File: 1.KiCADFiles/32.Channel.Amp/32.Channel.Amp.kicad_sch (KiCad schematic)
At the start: 4 parts

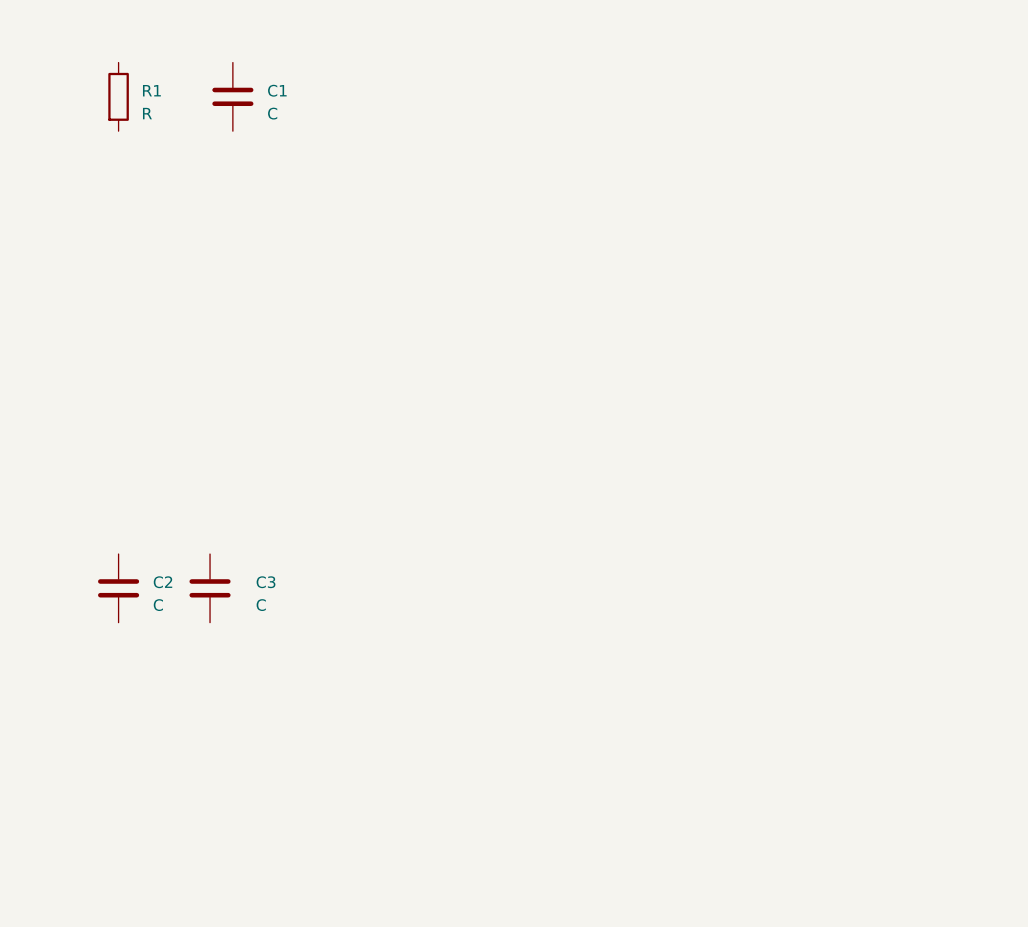
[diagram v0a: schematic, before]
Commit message: Created 16 Channel Box
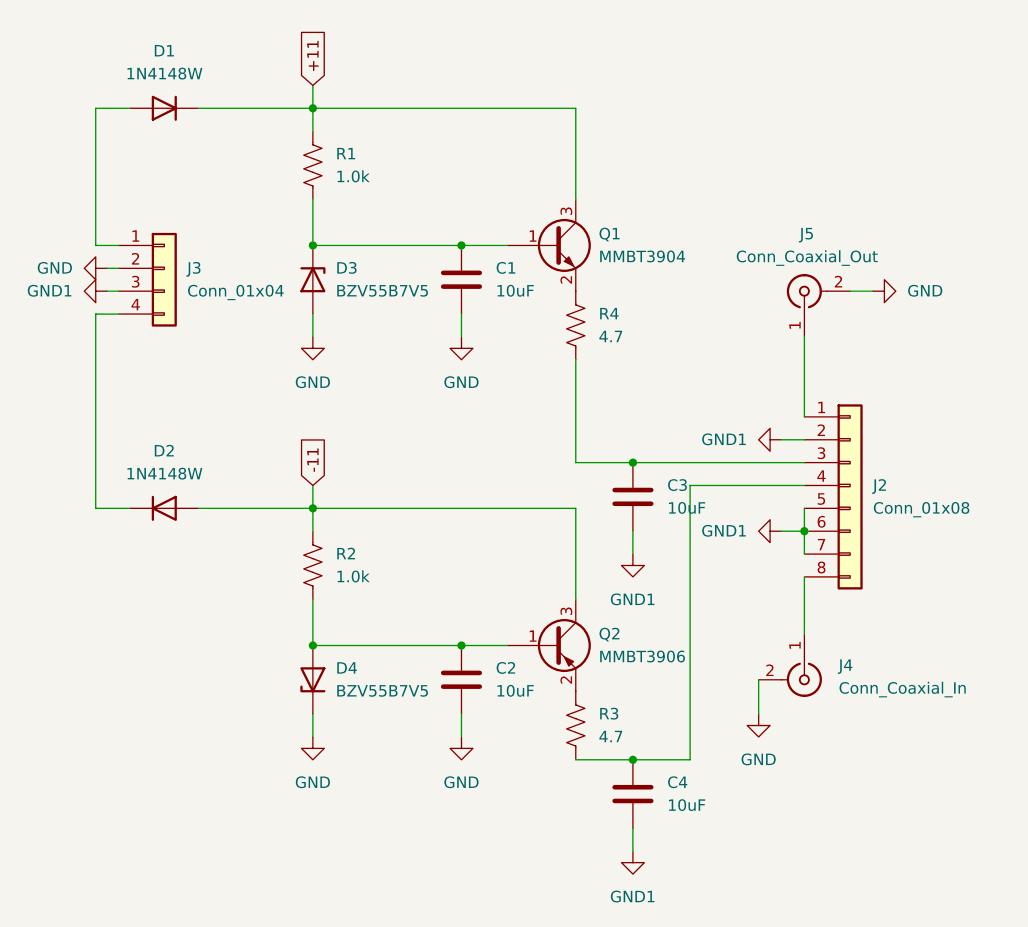
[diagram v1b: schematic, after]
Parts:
- removed R1: R, symbol Device:R
- added C4: 10uF, Capacitor_SMD:C_1206_3216Metric_Pad1.33x1.80mm_HandSolder, symbol Device:C
- added D1, D2: 1N4148W, Diode_SMD:D_SOD-123, symbol Diode:1N4148W
- added D3, D4: BZV55B7V5, Diode_SMD:D_MiniMELF, symbol Diode:BZV55B7V5
- added J2: Conn_01x08, Connector_PinSocket_2.54mm:PinSocket_1x08_P2.54mm_Vertical, symbol Connector_Generic:Conn_01x08
- added J3: Conn_01x04, Connector_PinSocket_2.54mm:PinSocket_1x04_P2.54mm_Vertical, symbol Connector_Generic:Conn_01x04
- added J4: Conn_Coaxial_In, Connector_Coaxial:SMA_Amphenol_901-144_Vertical, symbol Connector:Conn_Coaxial
- added J5: Conn_Coaxial_Out, Connector_Coaxial:SMA_Amphenol_901-144_Vertical, symbol Connector:Conn_Coaxial
- added Q1: MMBT3904, Package_TO_SOT_SMD:SOT-23, symbol Transistor_BJT:MMBT3904
- added Q2: MMBT3906, Package_TO_SOT_SMD:SOT-23, symbol Transistor_BJT:MMBT3906
- added R1, R2: 1.0k, Resistor_SMD:R_1206_3216Metric_Pad1.30x1.75mm_HandSolder, symbol Device:R_US
- added R3, R4: 4.7, Resistor_SMD:R_1206_3216Metric_Pad1.30x1.75mm_HandSolder, symbol Device:R_US
- C1, C2, C3: value C -> 10uF; footprint (none) -> Capacitor_SMD:C_1206_3216Metric_Pad1.33x1.80mm_HandSolder
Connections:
- net at C3.1: now also J2.3 (Pin_3), R4.2
- net GND1: now reaches C3.2
- net GND1: now also C4.2, J2.2 (GND), J2.5 (Pin_5), J2.6 (Pin_6), J2.7 (Pin_7), J3.3 (Pin_3)
- net at C1.1: now also D3.1 (K), Q1.1 (B), R1.2
- net GND: now reaches C1.2
- net GND: now also C2.2, D3.2 (A), D4.1 (K), J3.2 (Pin_2), J4.2 (Ext), J5.2 (Ext)
- net at C2.1: now also D4.2 (A), Q2.1 (B), R2.2
- new net: C4.1, J2.4 (Pin_4), R3.2
- new net: Q2.2 (E), R3.1
- new net: D1.2 (A), J3.1 (Pin_1)
- new net: J2.8 (Input), J4.1 (In)
- new net: J2.1 (Output), J5.1 (In)
- new net: D2.1 (K), J3.4 (Pin_4)
- new net: Q1.2 (E), R4.1
- new net +11: D1.1 (K), Q1.3 (C), R1.1
- new net -11: D2.2 (A), Q2.3 (C), R2.1

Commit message: Updated 32 Channel Format, Included Chip Board
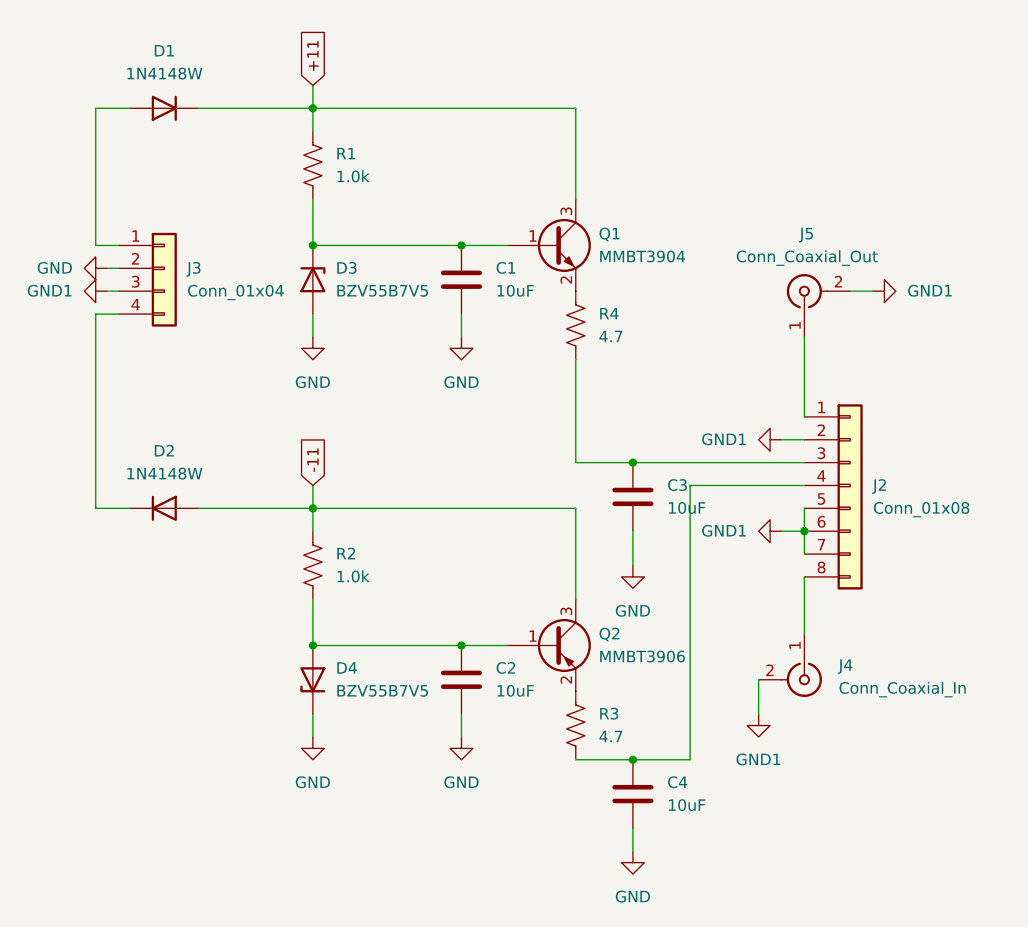
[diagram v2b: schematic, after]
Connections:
- net GND: now also C3.2, C4.2; no longer J4.2 (Ext), J5.2 (Ext)
- net GND1: now also J4.2 (Ext), J5.2 (Ext); no longer C3.2, C4.2
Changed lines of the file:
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@@
     (stroke (width 0) (type default))
   )
-  (wire (pts (xy 99.06 86.36) (xy 99.06 83.82))
+  (wire (pts (xy 99.06 87.63) (xy 99.06 83.82))
     (stroke (width 0) (type default))
   )
@@
     )
   )
+  (symbol (lib_id "power:GND1") (at 125.73 57.15 90) (unit 1)
+    (in_bom yes) (on_board yes) (dnp no) (fields_autoplaced)
+    (property "Reference" "#PWR011" (at 132.08 57.15 0)
+      (effects (font (size 1.27 1.27)) hide)
+    )
+    (property "Value" "GND1" (at 129.54 57.15 90)
+      (effects (font (size 1.27 1.27)) (justify right))
+    )
+    (property "Footprint" "" (at 125.73 57.15 0)
+      (effects (font (size 1.27 1.27)) hide)
+    )
+    (property "Datasheet" "" (at 125.73 57.15 0)
+      (effects (font (size 1.27 1.27)) hide)
+    )
+    (pin "1")
+    (instances
+      (project "Single.Channel.Amp"
+        (path "/08e8a37f-dc9c-4c12-ad59-7a5b52f61be7"
+          (reference "#PWR011") (unit 1)
+        )
+      )
+      (project "32.Channel.Amp"
+        (path "/13fa3f73-84bf-4039-afd1-d465267c6ba6"
+          (reference "#PWR08") (unit 1)
+        )
+      )
+    )
+  )
   (symbol (lib_id "Device:C") (at 99.06 113.03 0) (unit 1)
     (in_bom yes) (on_board yes) (dnp no) (fields_autoplaced)
@@
     )
   )
+  (symbol (lib_id "power:GND") (at 99.06 87.63 0) (unit 1)
+    (in_bom yes) (on_board yes) (dnp no) (fields_autoplaced)
+    (property "Reference" "#PWR02" (at 99.06 93.98 0)
+      (effects (font (size 1.27 1.27)) hide)
+    )
+    (property "Value" "GND" (at 99.06 92.71 0)
+      (effects (font (size 1.27 1.27)))
+    )
+    (property "Footprint" "" (at 99.06 87.63 0)
+      (effects (font (size 1.27 1.27)) hide)
+    )
+    (property "Datasheet" "" (at 99.06 87.63 0)
+      (effects (font (size 1.27 1.27)) hide)
+    )
+    (pin "1")
+    (instances
+      (project "Single.Channel.Amp"
+        (path "/08e8a37f-dc9c-4c12-ad59-7a5b52f61be7"
+          (reference "#PWR02") (unit 1)
+        )
+      )
+      (project "32.Channel.Amp"
+        (path "/13fa3f73-84bf-4039-afd1-d465267c6ba6"
+          (reference "#PWR09") (unit 1)
+        )
+      )
+    )
+  )
   (symbol (lib_id "Connector:Conn_Coaxial") (at 118.11 57.15 90) (unit 1)
     (in_bom yes) (on_board yes) (dnp no) (fields_autoplaced)
@@
     )
   )
-  (symbol (lib_id "power:GND1") (at 99.06 119.38 0) (unit 1)
-    (in_bom yes) (on_board yes) (dnp no) (fields_autoplaced)
-    (property "Reference" "#PWR011" (at 99.06 125.73 0)
-      (effects (font (size 1.27 1.27)) hide)
-    )
-    (property "Value" "GND1" (at 99.06 124.46 0)
+  (symbol (lib_id "Diode:1N4148W") (at 46.99 81.28 0) (unit 1)
+    (in_bom yes) (on_board yes) (dnp no) (fields_autoplaced)
+    (property "Reference" "D2" (at 46.99 74.93 0)
+      (effects (font (size 1.27 1.27)))
+    )
+    (property "Value" "1N4148W" (at 46.99 77.47 0)
+      (effects (font (size 1.27 1.27)))
+    )
+    (property "Footprint" "Diode_SMD:D_SOD-123" (at 46.99 85.725 0)
+      (effects (font (size 1.27 1.27)) hide)
+    )
+    (property "Datasheet" "https://www.vishay.com/docs/85748/1n4148w.pdf" (at 46.99 81.28 0)
+      (effects (font (size 1.27 1.27)) hide)
+    )
+    (property "Sim.Device" "D" (at 46.99 81.28 0)
+      (effects (font (size 1.27 1.27)) hide)
+    )
+    (property "Sim.Pins" "1=K 2=A" (at 46.99 81.28 0)
+      (effects (font (size 1.27 1.27)) hide)
+    )
+    (pin "1")
+    (pin "2")
+    (instances
+      (project "Single.Channel.Amp"
+        (path "/08e8a37f-dc9c-4c12-ad59-7a5b52f61be7"
+          (reference "D2") (unit 1)
+        )
+      )
+      (project "32.Channel.Amp"
+        (path "/13fa3f73-84bf-4039-afd1-d465267c6ba6"
+          (reference "D2") (unit 1)
+        )
+      )
+    )
+  )
+  (symbol (lib_id "power:GND") (at 99.06 119.38 0) (unit 1)
+    (in_bom yes) (on_board yes) (dnp no) (fields_autoplaced)
+    (property "Reference" "#PWR02" (at 99.06 125.73 0)
+      (effects (font (size 1.27 1.27)) hide)
+    )
+    (property "Value" "GND" (at 99.06 124.46 0)
       (effects (font (size 1.27 1.27)))
     )
@@
       (project "Single.Channel.Amp"
         (path "/08e8a37f-dc9c-4c12-ad59-7a5b52f61be7"
-          (reference "#PWR011") (unit 1)
-        )
-      )
-      (project "32.Channel.Amp"
-        (path "/13fa3f73-84bf-4039-afd1-d465267c6ba6"
-          (reference "#PWR08") (unit 1)
-        )
-      )
-    )
-  )
-  (symbol (lib_id "Diode:1N4148W") (at 46.99 81.28 0) (unit 1)
-    (in_bom yes) (on_board yes) (dnp no) (fields_autoplaced)
-    (property "Reference" "D2" (at 46.99 74.93 0)
-      (effects (font (size 1.27 1.27)))
-    )
-    (property "Value" "1N4148W" (at 46.99 77.47 0)
-      (effects (font (size 1.27 1.27)))
-    )
-    (property "Footprint" "Diode_SMD:D_SOD-123" (at 46.99 85.725 0)
-      (effects (font (size 1.27 1.27)) hide)
-    )
-    (property "Datasheet" "https://www.vishay.com/docs/85748/1n4148w.pdf" (at 46.99 81.28 0)
-      (effects (font (size 1.27 1.27)) hide)
-    )
-    (property "Sim.Device" "D" (at 46.99 81.28 0)
-      (effects (font (size 1.27 1.27)) hide)
-    )
-    (property "Sim.Pins" "1=K 2=A" (at 46.99 81.28 0)
-      (effects (font (size 1.27 1.27)) hide)
-    )
-    (pin "1")
-    (pin "2")
-    (instances
-      (project "Single.Channel.Amp"
-        (path "/08e8a37f-dc9c-4c12-ad59-7a5b52f61be7"
-          (reference "D2") (unit 1)
-        )
-      )
-      (project "32.Channel.Amp"
-        (path "/13fa3f73-84bf-4039-afd1-d465267c6ba6"
-          (reference "D2") (unit 1)
+          (reference "#PWR02") (unit 1)
+        )
+      )
+      (project "32.Channel.Amp"
+        (path "/13fa3f73-84bf-4039-afd1-d465267c6ba6"
+          (reference "#PWR012") (unit 1)
         )
       )
@@
         (path "/13fa3f73-84bf-4039-afd1-d465267c6ba6"
           (reference "J1") (unit 1)
-        )
-      )
-    )
-  )
-  (symbol (lib_id "power:GND") (at 113.03 104.14 0) (unit 1)
-    (in_bom yes) (on_board yes) (dnp no) (fields_autoplaced)
-    (property "Reference" "#PWR08" (at 113.03 110.49 0)
-      (effects (font (size 1.27 1.27)) hide)
-    )
-    (property "Value" "GND" (at 113.03 109.22 0)
-      (effects (font (size 1.27 1.27)))
-    )
-    (property "Footprint" "" (at 113.03 104.14 0)
-      (effects (font (size 1.27 1.27)) hide)
-    )
-    (property "Datasheet" "" (at 113.03 104.14 0)
-      (effects (font (size 1.27 1.27)) hide)
-    )
-    (pin "1")
-    (instances
-      (project "Single.Channel.Amp"
-        (path "/08e8a37f-dc9c-4c12-ad59-7a5b52f61be7"
-          (reference "#PWR08") (unit 1)
-        )
-      )
-      (project "32.Channel.Amp"
-        (path "/13fa3f73-84bf-4039-afd1-d465267c6ba6"
-          (reference "#PWR09") (unit 1)
         )
       )
@@
     )
   )
-  (symbol (lib_id "power:GND") (at 125.73 57.15 90) (unit 1)
-    (in_bom yes) (on_board yes) (dnp no) (fields_autoplaced)
-    (property "Reference" "#PWR09" (at 132.08 57.15 0)
-      (effects (font (size 1.27 1.27)) hide)
-    )
-    (property "Value" "GND" (at 129.54 57.15 90)
-      (effects (font (size 1.27 1.27)) (justify right))
-    )
-    (property "Footprint" "" (at 125.73 57.15 0)
-      (effects (font (size 1.27 1.27)) hide)
-    )
-    (property "Datasheet" "" (at 125.73 57.15 0)
-      (effects (font (size 1.27 1.27)) hide)
-    )
-    (pin "1")
-    (instances
-      (project "Single.Channel.Amp"
-        (path "/08e8a37f-dc9c-4c12-ad59-7a5b52f61be7"
-          (reference "#PWR09") (unit 1)
-        )
-      )
-      (project "32.Channel.Amp"
-        (path "/13fa3f73-84bf-4039-afd1-d465267c6ba6"
-          (reference "#PWR012") (unit 1)
-        )
-      )
-    )
-  )
   (symbol (lib_id "power:GND") (at 80.01 62.23 0) (unit 1)
     (in_bom yes) (on_board yes) (dnp no) (fields_autoplaced)
@@
     )
   )
+  (symbol (lib_id "power:GND1") (at 113.03 104.14 0) (unit 1)
+    (in_bom yes) (on_board yes) (dnp no) (fields_autoplaced)
+    (property "Reference" "#PWR011" (at 113.03 110.49 0)
+      (effects (font (size 1.27 1.27)) hide)
+    )
+    (property "Value" "GND1" (at 113.03 109.22 0)
+      (effects (font (size 1.27 1.27)))
+    )
+    (property "Footprint" "" (at 113.03 104.14 0)
+      (effects (font (size 1.27 1.27)) hide)
+    )
+    (property "Datasheet" "" (at 113.03 104.14 0)
+      (effects (font (size 1.27 1.27)) hide)
+    )
+    (pin "1")
+    (instances
+      (project "Single.Channel.Amp"
+        (path "/08e8a37f-dc9c-4c12-ad59-7a5b52f61be7"
+          (reference "#PWR011") (unit 1)
+        )
+      )
+      (project "32.Channel.Amp"
+        (path "/13fa3f73-84bf-4039-afd1-d465267c6ba6"
+          (reference "#PWR07") (unit 1)
+        )
+      )
+    )
+  )
   (symbol (lib_id "Diode:BZV55B7V5") (at 63.5 100.33 90) (unit 1)
     (in_bom yes) (on_board yes) (dnp no) (fields_autoplaced)
@@
         )
       )
-    )
-  )
-  (symbol (lib_id "power:GND1") (at 99.06 86.36 0) (unit 1)
-    (in_bom yes) (on_board yes) (dnp no) (fields_autoplaced)
-    (property "Reference" "#PWR012" (at 99.06 92.71 0)
-      (effects (font (size 1.27 1.27)) hide)
-    )
-    (property "Value" "GND1" (at 99.06 91.44 0)
-      (effects (font (size 1.27 1.27)))
-    )
-    (property "Footprint" "" (at 99.06 86.36 0)
-      (effects (font (size 1.27 1.27)) hide)
-    )
-    (property "Datasheet" "" (at 99.06 86.36 0)
-      (effects (font (size 1.27 1.27)) hide)
-    )
-    (pin "1")
-    (instances
-      (project "Single.Channel.Amp"
-        (path "/08e8a37f-dc9c-4c12-ad59-7a5b52f61be7"
-          (reference "#PWR012") (unit 1)
-        )
-      )
-      (project "32.Channel.Amp"
-        (path "/13fa3f73-84bf-4039-afd1-d465267c6ba6"
-          (reference "#PWR07") (unit 1)
-        )
-      )
